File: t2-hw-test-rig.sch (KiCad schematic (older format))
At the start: 51 parts, among them J101 CONN_01X02, J102 BARREL_JACK, J103 CONN_01X02, P101 5VDC POWER, P102 USB A TO MicroUSB A CABLE, P103 USB A TO MicroUSB A CABLE, P104 ETHERNET CABLE, P105 USB THUMB DRIVE, P106 USB THUMB DRIVE, Q101 pMOS, U101 MAX6102, U102 XC6206P332MR-G

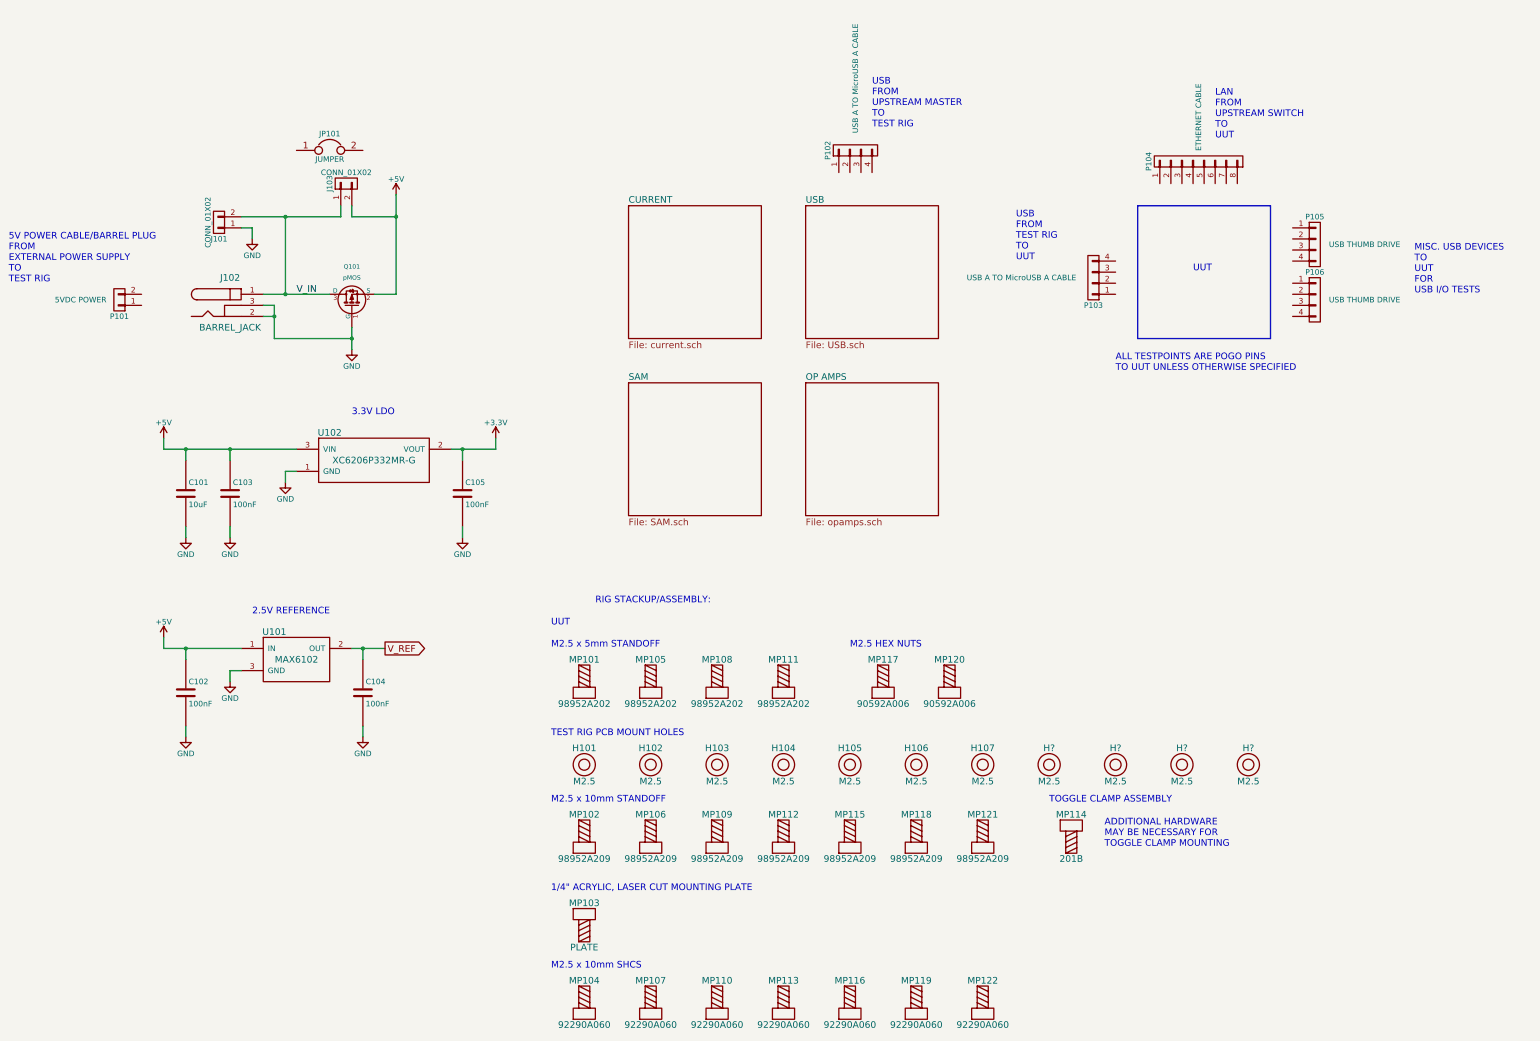
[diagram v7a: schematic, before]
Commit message: moved mechanicals to a separate sheet
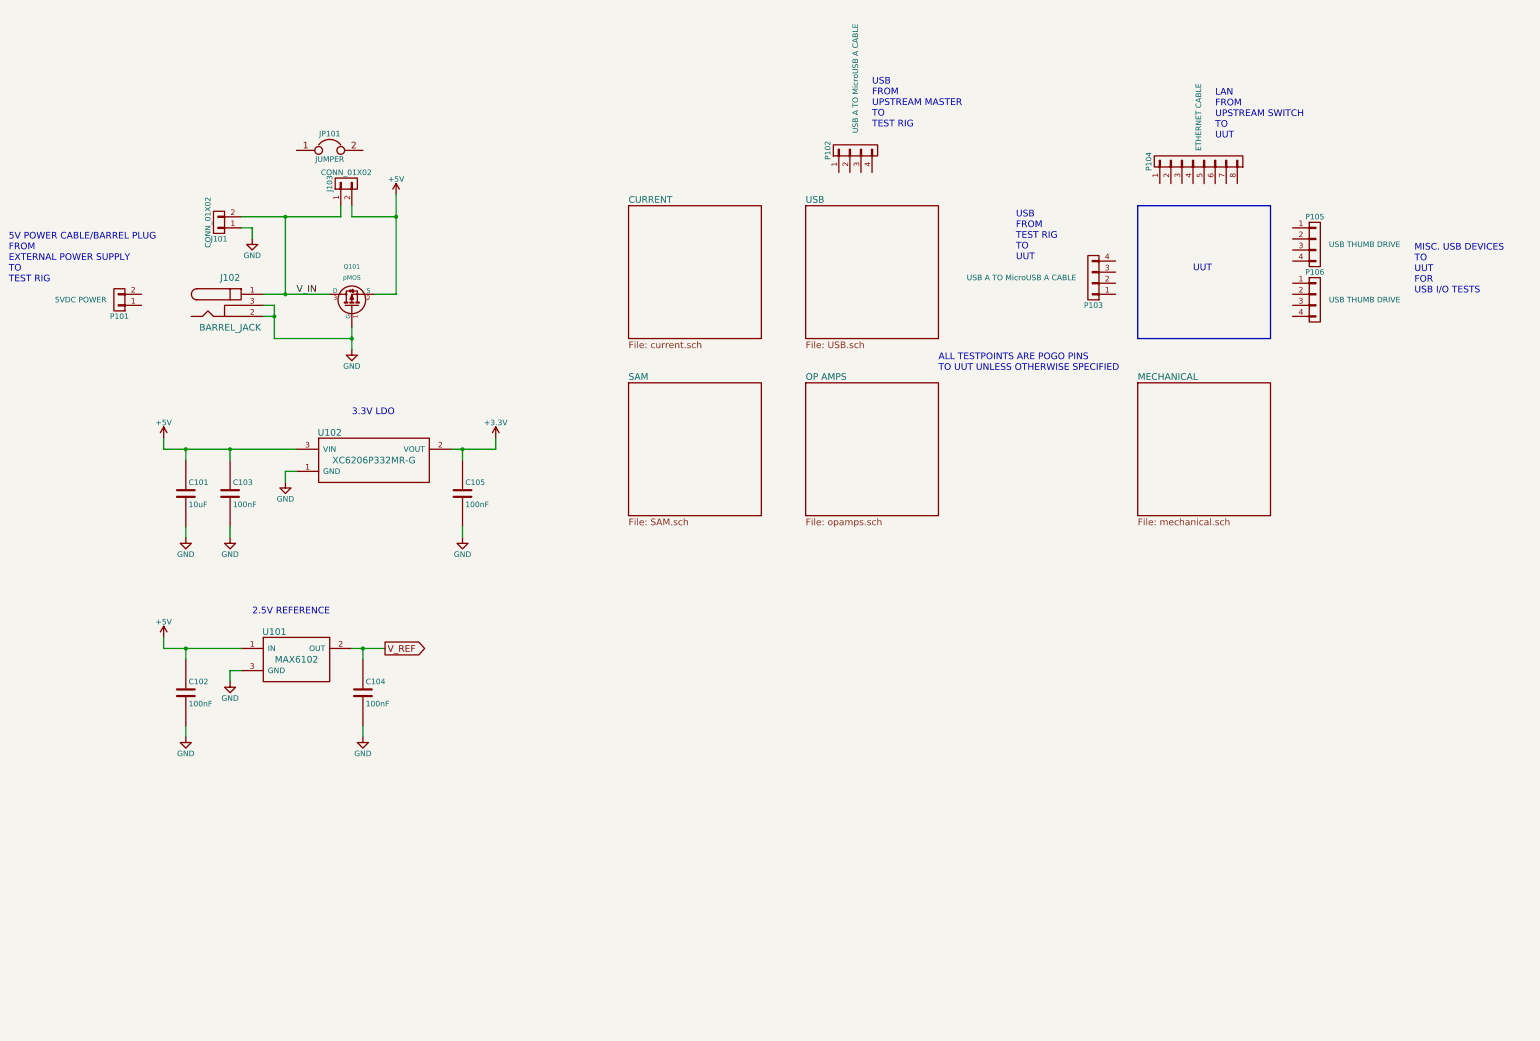
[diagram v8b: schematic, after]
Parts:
- removed H101, H102, H103, H104, H105, H106, H107, H? (x4): M2.5, tm-kicad-lib:MountingHole_2-5mm, symbol HOLE
- removed MP101, MP105, MP108, MP111: 98952A202, symbol MECHANICAL
- removed MP102, MP106, MP109, MP112, MP115, MP118, MP121: 98952A209, symbol MECHANICAL
- removed MP103: PLATE, symbol MECHANICAL
- removed MP104, MP107, MP110, MP113, MP116, MP119, MP122: 92290A060, symbol MECHANICAL
- removed MP114: 201B, symbol MECHANICAL
- removed MP117, MP120: 90592A006, symbol MECHANICAL
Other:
- note removed: "1/4" ACRYLIC, LASER CUT MOUNTING PLATE"
- note removed: "ADDITIONAL HARDWARE\nMAY BE NECESSARY FOR\nTOGGLE CLAMP MOUNTING"
- note removed: "M2.5 HEX NUTS"
- note removed: "M2.5 x 10mm SHCS"
- note removed: "M2.5 x 10mm STANDOFF"
- note removed: "M2.5 x 5mm STANDOFF"
- note removed: "RIG STACKUP/ASSEMBLY:"
- note removed: "TEST RIG PCB MOUNT HOLES"
- note removed: "TOGGLE CLAMP ASSEMBLY"
